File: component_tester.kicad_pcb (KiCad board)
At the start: 2 copper layers, 70 x 48 mm, 86 parts, among them IC1 ATMEGA16U2, IC2 ATMEGA328P-A, P1 USB_OTG, P10 ICSP_prog_16u2_4, P11 BO_PC6, P12 ICSP_prog_16u2_5, P13 BO_PC5, P14 BO_PD2, P15 BO_PD3, P16 BO_PD4, P17 BO_PD5, P18 BO_PD6, P19 ICSP_prog_328_1, P2 BATTERY_CONNECTOR, P20 ICSP_prog_328_3, P21 ICSP_prog_328_4, P22 ICSP_prog_328_5, P23 CONN_01X01, P24 Device Under Test, P25 CONN_01X03, P3 Voltage_for_zener, P4 BO_PC7, P5 ICSP_prog_16u2_1, P6 BO_PD0, P7 BO_PD1, P8 BO_PC4, P9 ICSP_prog_16u2_3, Q1 TRANSISTOR_NPN_2N2222_KSP222A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, SW1 ON-OFF switch, SW2 DO_MEASUREMENT, SW3 CONNECT_CAP, U1 NCP1117ST50T3G, U2 XF2L-2625-1A, U3 LT1004, U4 CDSOT23-SRV05-4, Y1 8MHz, Y2 16MHz

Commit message: Added screw holes
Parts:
- added REF**: 1pin, Connect:1pin, F.Cu at (165.1, 127.6)
- added REF**: 1pin, Connect:1pin, F.Cu at (131.7, 103.4)
- added REF**: 1pin, Connect:1pin, F.Cu at (112.9, 143.9)
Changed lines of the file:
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@@
 (kicad_pcb (version 4) (host pcbnew 4.0.2+e4-6225~38~ubuntu16.04.1-stable)
   (general
-    (links 193)
+    (links 196)
     (no_connects 3)
-    (area 99.949999 99.949999 170.050001 148.050001)
+    (area 93.753 93.596447 170.970334 149.9968)
     (thickness 1.6)
     (drawings 4)
     (tracks 1061)
     (zones 0)
-    (modules 86)
+    (modules 89)
     (nets 77)
   )
@@
     (mod_text_size 1 1)
     (mod_text_width 0.15)
-    (pad_size 1.5 1.5)
-    (pad_drill 0.6)
+    (pad_size 4.064 4.064)
+    (pad_drill 3.048)
     (pad_to_mask_clearance 0)
     (aux_axis_origin 0 0)
@@
     (add_net UART_328_TO_16u)
   )
+  (module Connect:1pin (layer F.Cu)
+    (at 165.1 127.635)
+    (descr "module 1 pin (ou trou mecanique de percage)")
+    (tags DEV)
+    (fp_text reference REF** (at 0 -3.048) (layer F.SilkS)
+      (effects (font (size 1 1) (thickness 0.15)))
+    )
+    (fp_text value 1pin (at 0 2.794) (layer F.Fab)
+      (effects (font (size 1 1) (thickness 0.15)))
+    )
+    (fp_circle (center 0 0) (end 0 -2.286) (layer F.SilkS) (width 0.15))
+    (pad 1 thru_hole circle (at 0 0) (size 4.064 4.064) (drill 3.048) (layers *.Cu *.Mask F.SilkS)
+      (net 1 GND))
+  )
+  (module Connect:1pin (layer F.Cu)
+    (at 131.699 103.378)
+    (descr "module 1 pin (ou trou mecanique de percage)")
+    (tags DEV)
+    (fp_text reference REF** (at 0 -3.048) (layer F.SilkS)
+      (effects (font (size 1 1) (thickness 0.15)))
+    )
+    (fp_text value 1pin (at 0 2.794) (layer F.Fab)
+      (effects (font (size 1 1) (thickness 0.15)))
+    )
+    (fp_circle (center 0 0) (end 0 -2.286) (layer F.SilkS) (width 0.15))
+    (pad 1 thru_hole circle (at 0 0) (size 4.064 4.064) (drill 3.048) (layers *.Cu *.Mask F.SilkS)
+      (net 1 GND))
+  )
   (module drawn_by_jpmeijers:CONN_DUT (layer F.Cu)
     (at 149.8092 135.2296)
@@
     )
   )
+  (module Connect:1pin (layer F.Cu)
+    (at 112.903 143.891)
+    (descr "module 1 pin (ou trou mecanique de percage)")
+    (tags DEV)
+    (fp_text reference REF** (at 0 -3.048) (layer F.SilkS)
+      (effects (font (size 1 1) (thickness 0.15)))
+    )
+    (fp_text value 1pin (at 0 2.794) (layer F.Fab)
+      (effects (font (size 1 1) (thickness 0.15)))
+    )
+    (fp_circle (center 0 0) (end 0 -2.286) (layer F.SilkS) (width 0.15))
+    (pad 1 thru_hole circle (at 0 0) (size 4.064 4.064) (drill 3.048) (layers *.Cu *.Mask F.SilkS)
+      (net 1 GND))
+  )
   (gr_line (start 100 148) (end 170 148) (angle 90) (layer Edge.Cuts) (width 0.1))
   (gr_line (start 170 100) (end 170 148) (angle 90) (layer Edge.Cuts) (width 0.1))
@@
   (segment (start 105.3592 110.998) (end 107.3912 108.966) (width 0.25) (layer F.Cu) (net 6))
   (segment (start 103.144 110.998) (end 105.3592 110.998) (width 0.25) (layer F.Cu) (net 6))
-  (segment (start 140.335 130.957) (end 140.335 129.5146) (width 0.25) (layer B.Cu) (net 7) (status 400000))
+  (segment (start 140.335 130.957) (end 140.335 129.5146) (width 0.25) (layer B.Cu) (net 7))
   (segment (start 140.335 129.5146) (end 140.6144 129.2352) (width 0.25) (layer B.Cu) (net 7))
   (segment (start 138.75 132.715) (end 138.75 131.0996) (width 0.25) (layer F.Cu) (net 7))

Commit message: Fix capacitor values Added Vusb cap, fix unconnected nets, better grounding.
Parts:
- added C21: 100n, Capacitors_SMD:C_0805_HandSoldering, B.Cu at (131.1, 115.4)
- C10, C9: value 10uF -> 10u
- C15, C16: value 22pF -> 22p
- C3: value 1uF -> 1u
- moved U4 0.11 mm to (153.5, 132.5)
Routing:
- net /Reference_voltage: track 32.8 -> 35.9 mm
- net /RESET_16u: track 6.27 -> 9.16 mm
- net GND: track 576.6 -> 579.5 mm, vias 125 -> 126
- net /USB_Vcc: track 52.0 -> 53.8 mm, vias 4 -> 5
- net UART_328_TO_16u: track 58.2 -> 58.8 mm
- net /LCD_DATA_B2: track 12.5 -> 11.9 mm

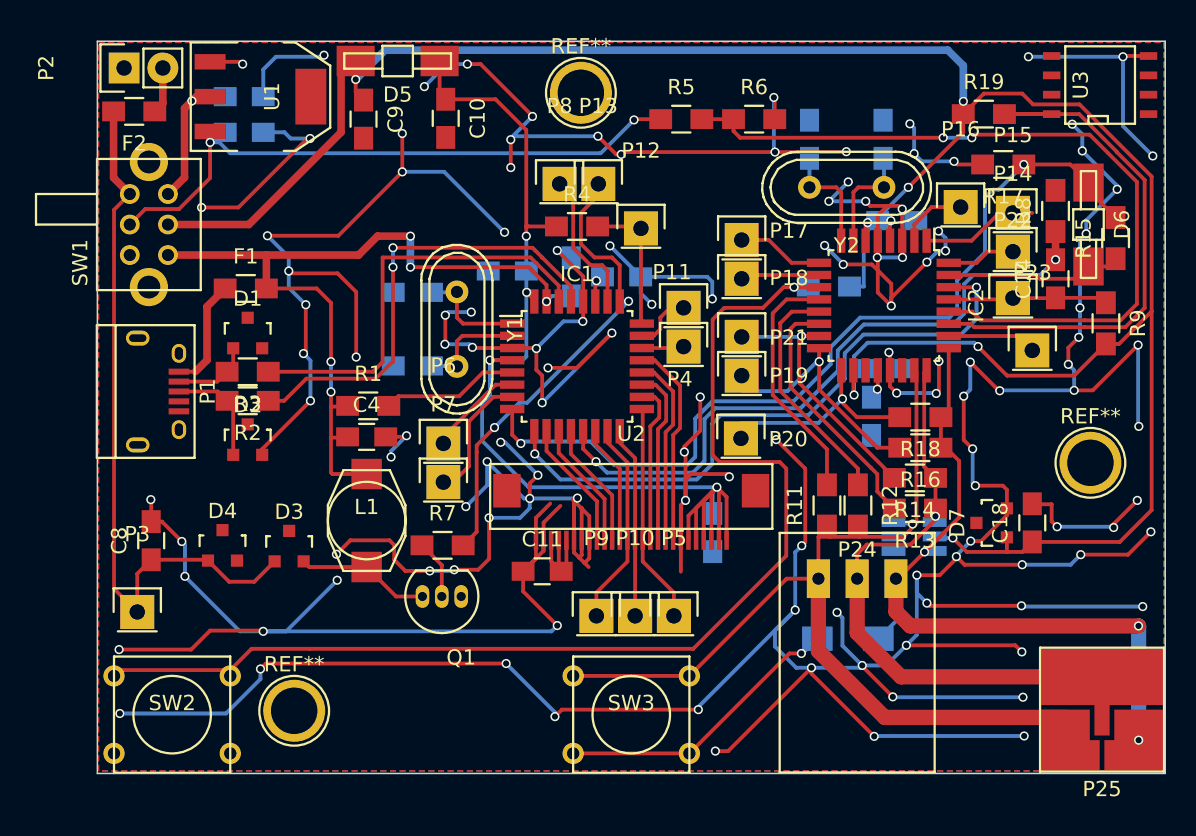
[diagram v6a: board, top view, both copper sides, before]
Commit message: Move component references on silkscreen to be more readable.
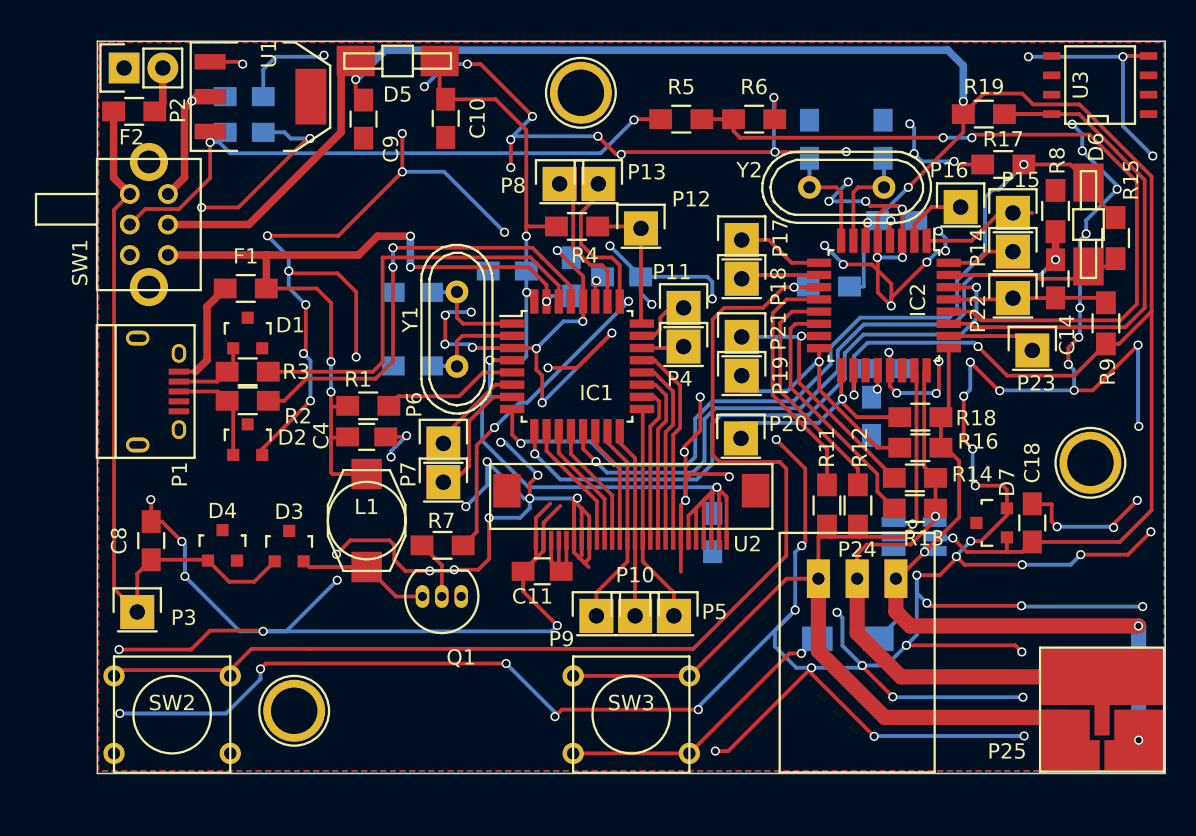
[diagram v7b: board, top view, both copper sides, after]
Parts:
- renumbered REF** to ?

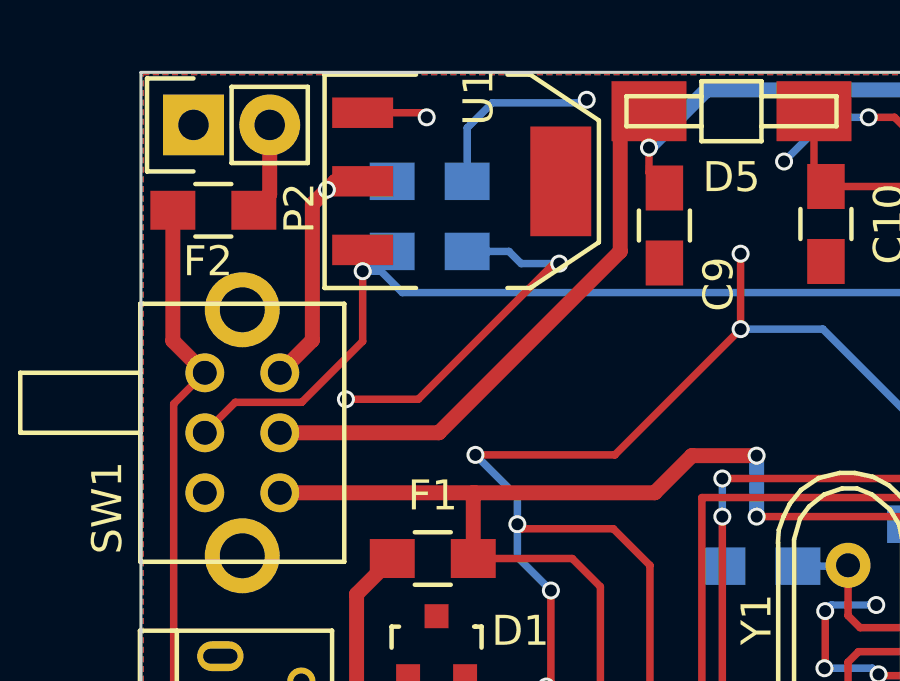
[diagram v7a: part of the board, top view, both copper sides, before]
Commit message: Added voltage regulator option
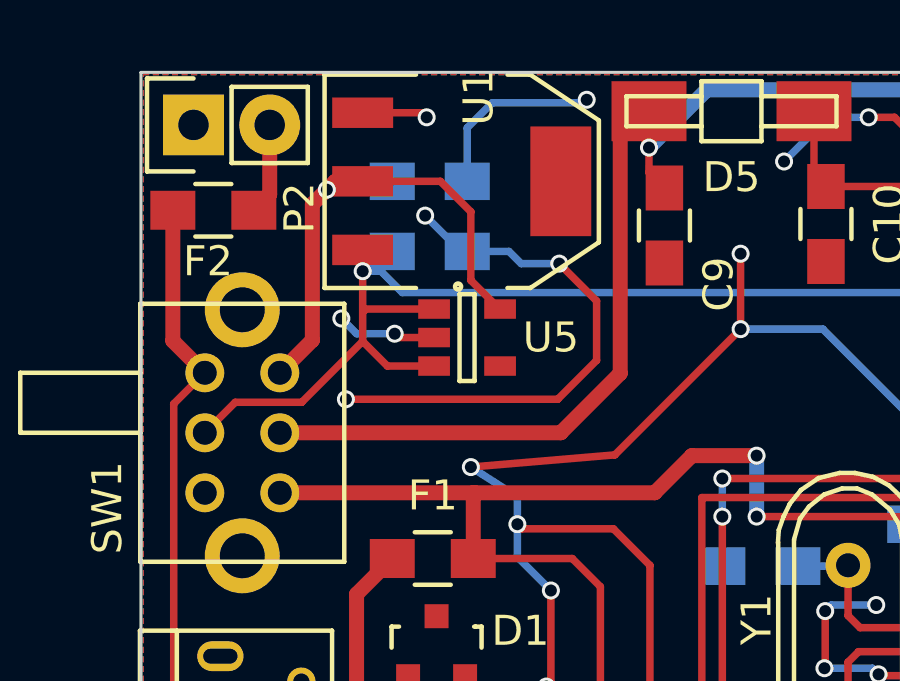
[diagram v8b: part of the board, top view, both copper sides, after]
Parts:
- added U5: LP2985LV, TO_SOT_Packages_SMD:SOT-23-5, F.Cu at (110.9, 108.8)
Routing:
- net GND: track 579.5 -> 588.6 mm, vias 126 -> 129
- net /Volt_reg_5v: track 10.4 -> 18.0 mm
- net Batt_Switch: track 41.6 -> 46.8 mm
- net 5Volt_328: track 168.3 -> 170.7 mm
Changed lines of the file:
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@@
 (kicad_pcb (version 4) (host pcbnew 4.0.2+e4-6225~38~ubuntu16.04.1-stable)
   (general
-    (links 198)
+    (links 202)
     (no_connects 1)
-    (area 93.753 93.596447 170.970334 149.9968)
+    (area 99.949999 99.949999 170.050001 148.050001)
     (thickness 1.6)
     (drawings 4)
-    (tracks 1071)
+    (tracks 1094)
     (zones 0)
-    (modules 90)
-    (nets 77)
+    (modules 91)
+    (nets 78)
   )
   (page A4)
@@
   (net 75 "Net-(U4-Pad1)")
   (net 76 Battery_fused)
+  (net 77 "Net-(U5-Pad4)")
   (net_class Default "This is the default net class."
     (clearance 0.2)
@@
     (add_net "Net-(U3-Pad7)")
     (add_net "Net-(U4-Pad1)")
+    (add_net "Net-(U5-Pad4)")
     (add_net UART_16u_TO_328)
     (add_net UART_328_TO_16u)
@@
     )
   )
+  (module TO_SOT_Packages_SMD:SOT-23-5 (layer F.Cu)
+    (at 110.871 108.839)
+    (descr "5-pin SOT23 package")
+    (tags SOT-23-5)
+    (attr smd)
+    (fp_text reference U5 (at 2.794 0) (layer F.SilkS)
+      (effects (font (size 1 1) (thickness 0.15)))
+    )
+    (fp_text value LP2985LV (at -0.05 2.35) (layer F.Fab)
+      (effects (font (size 1 1) (thickness 0.15)))
+    )
+    (fp_line (start -1.8 -1.6) (end 1.8 -1.6) (layer F.CrtYd) (width 0.05))
+    (fp_line (start 1.8 -1.6) (end 1.8 1.6) (layer F.CrtYd) (width 0.05))
+    (fp_line (start 1.8 1.6) (end -1.8 1.6) (layer F.CrtYd) (width 0.05))
+    (fp_line (start -1.8 1.6) (end -1.8 -1.6) (layer F.CrtYd) (width 0.05))
+    (fp_circle (center -0.3 -1.7) (end -0.2 -1.7) (layer F.SilkS) (width 0.15))
+    (fp_line (start 0.25 -1.45) (end -0.25 -1.45) (layer F.SilkS) (width 0.15))
+    (fp_line (start 0.25 1.45) (end 0.25 -1.45) (layer F.SilkS) (width 0.15))
+    (fp_line (start -0.25 1.45) (end 0.25 1.45) (layer F.SilkS) (width 0.15))
+    (fp_line (start -0.25 -1.45) (end -0.25 1.45) (layer F.SilkS) (width 0.15))
+    (pad 1 smd rect (at -1.1 -0.95) (size 1.06 0.65) (layers F.Cu F.Paste F.Mask)
+      (net 6 Batt_Switch))
+    (pad 2 smd rect (at -1.1 0) (size 1.06 0.65) (layers F.Cu F.Paste F.Mask)
+      (net 1 GND))
+    (pad 3 smd rect (at -1.1 0.95) (size 1.06 0.65) (layers F.Cu F.Paste F.Mask)
+      (net 6 Batt_Switch))
+    (pad 4 smd rect (at 1.1 0.95) (size 1.06 0.65) (layers F.Cu F.Paste F.Mask)
+      (net 77 "Net-(U5-Pad4)"))
+    (pad 5 smd rect (at 1.1 -0.95) (size 1.06 0.65) (layers F.Cu F.Paste F.Mask)
+      (net 8 /Volt_reg_5v))
+    (model TO_SOT_Packages_SMD.3dshapes/SOT-23-5.wrl
+      (at (xyz 0 0 0))
+      (scale (xyz 1 1 1))
+      (rotate (xyz 0 0 0))
+    )
+  )
   (gr_line (start 100 148) (end 170 148) (angle 90) (layer Edge.Cuts) (width 0.1))
   (gr_line (start 170 100) (end 170 148) (angle 90) (layer Edge.Cuts) (width 0.1))
   (gr_line (start 100 100) (end 100 148) (angle 90) (layer Edge.Cuts) (width 0.1))
   (gr_line (start 100 100) (end 170 100) (angle 90) (layer Edge.Cuts) (width 0.1))
+  (segment (start 110.8764 105.9688) (end 110.6678 105.9688) (width 0.25) (layer B.Cu) (net 1))
+  (segment (start 110.6678 105.9688) (end 109.474 104.775) (width 0.25) (layer B.Cu) (net 1))
+  (via (at 109.474 104.775) (size 0.6) (drill 0.4) (layers F.Cu B.Cu) (net 1))
+  (segment (start 108.458 108.712) (end 107.188 108.712) (width 0.25) (layer B.Cu) (net 1))
+  (segment (start 108.585 108.839) (end 108.458 108.712) (width 0.25) (layer F.Cu) (net 1))
+  (via (at 108.458 108.712) (size 0.6) (drill 0.4) (layers F.Cu B.Cu) (net 1))
+  (segment (start 109.771 108.839) (end 108.585 108.839) (width 0.25) (layer F.Cu) (net 1))
+  (via (at 106.68 108.204) (size 0.6) (drill 0.4) (layers F.Cu B.Cu) (net 1))
+  (segment (start 107.188 108.712) (end 106.68 108.204) (width 0.25) (layer B.Cu) (net 1))
+  (segment (start 106.8324 110.8964) (end 113.8936 110.8964) (width 0.25) (layer F.Cu) (net 1))
+  (via (at 106.8324 110.8964) (size 0.6) (drill 0.4) (layers F.Cu B.Cu) (net 1))
+  (segment (start 115.189 107.6198) (end 113.9444 106.3752) (width 0.25) (layer F.Cu) (net 1))
+  (segment (start 115.189 109.601) (end 115.189 107.6198) (width 0.25) (layer F.Cu) (net 1))
+  (segment (start 113.8936 110.8964) (end 115.189 109.601) (width 0.25) (layer F.Cu) (net 1))
   (segment (start 135.616 115.443) (end 135.616 115.423) (width 0.25) (layer B.Cu) (net 1))
   (segment (start 135.616 115.423) (end 133.604 113.411) (width 0.25) (layer B.Cu) (net 1))
@@
   (via (at 113.9444 106.3752) (size 0.6) (drill 0.4) (layers F.Cu B.Cu) (net 1))
   (segment (start 110.8764 105.9688) (end 112.268 105.9688) (width 0.25) (layer B.Cu) (net 1))
-  (via (at 106.8324 110.8964) (size 0.6) (drill 0.4) (layers F.Cu B.Cu) (net 1))
-  (segment (start 109.2454 110.8964) (end 106.8324 110.8964) (width 0.25) (layer F.Cu) (net 1))
-  (segment (start 113.7666 106.3752) (end 109.2454 110.8964) (width 0.25) (layer F.Cu) (net 1))
   (segment (start 107.3912 101.346) (end 109.3724 101.346) (width 0.25) (layer F.Cu) (net 1))
   (via (at 109.5248 101.4984) (size 0.6) (drill 0.4) (layers F.Cu B.Cu) (net 1))
@@
   (segment (start 115.7986 112.7506) (end 119.9896 108.5596) (width 0.25) (layer F.Cu) (net 1))
   (segment (start 112.5474 114.1476) (end 112.5474 115.062) (width 0.25) (layer B.Cu) (net 1))
-  (via (at 111.1504 112.7506) (size 0.6) (drill 0.4) (layers F.Cu B.Cu) (net 1))
-  (segment (start 112.5474 114.1476) (end 111.1504 112.7506) (width 0.25) (layer B.Cu) (net 1))
-  (segment (start 111.1504 112.7506) (end 115.7986 112.7506) (width 0.25) (layer F.Cu) (net 1))
+  (via (at 110.998 113.157) (size 0.6) (drill 0.4) (layers F.Cu B.Cu) (net 1))
+  (segment (start 112.5474 114.1476) (end 110.998 113.157) (width 0.25) (layer B.Cu) (net 1))
+  (segment (start 110.998 113.157) (end 115.7986 112.7506) (width 0.25) (layer F.Cu) (net 1))
   (via (at 119.9896 106.045) (size 0.6) (drill 0.4) (layers F.Cu B.Cu) (net 1))
   (segment (start 113.9698 123.571) (end 113.9698 120.9294) (width 0.25) (layer B.Cu) (net 1))
@@
   (segment (start 129.445 115.983) (end 128.5875 115.1255) (width 0.25) (layer F.Cu) (net 5))
   (segment (start 128.5875 115.1255) (end 128.524 115.062) (width 0.25) (layer F.Cu) (net 5))
+  (segment (start 109.771 109.789) (end 108.2142 109.789) (width 0.25) (layer F.Cu) (net 6))
+  (segment (start 108.2142 109.789) (end 107.3912 108.966) (width 0.25) (layer F.Cu) (net 6))
+  (segment (start 109.771 107.889) (end 107.3912 107.889) (width 0.25) (layer F.Cu) (net 6))
+  (segment (start 107.442 107.95) (end 107.3912 107.95) (width 0.25) (layer F.Cu) (net 6))
+  (segment (start 107.442 107.9398) (end 107.442 107.95) (width 0.25) (layer F.Cu) (net 6))
+  (segment (start 107.3912 107.889) (end 107.442 107.9398) (width 0.25) (layer F.Cu) (net 6))
   (segment (start 107.3912 106.6292) (end 108.0008 106.6292) (width 0.25) (layer B.Cu) (net 6))
   (segment (start 135.2296 105.1052) (end 136.9276 105.1052) (width 0.25) (layer F.Cu) (net 6))
@@
   (segment (start 108.0516 105.9688) (end 108.3764 105.9688) (width 0.25) (layer B.Cu) (net 6))
   (segment (start 102.128 112.014) (end 103.144 110.998) (width 0.25) (layer F.Cu) (net 6))
-  (segment (start 107.3912 108.966) (end 107.3912 106.6292) (width 0.25) (layer F.Cu) (net 6))
+  (segment (start 107.3912 108.966) (end 107.3912 107.95) (width 0.25) (layer F.Cu) (net 6))
+  (segment (start 107.3912 107.95) (end 107.3912 106.6292) (width 0.25) (layer F.Cu) (net 6))
   (segment (start 107.3912 106.6292) (end 107.3912 105.918) (width 0.25) (layer F.Cu) (net 6))
   (segment (start 105.3592 110.998) (end 107.3912 108.966) (width 0.25) (layer F.Cu) (net 6))
@@
   (segment (start 128.651 115.316) (end 128.397 115.062) (width 0.25) (layer B.Cu) (net 7))
   (segment (start 128.397 115.062) (end 128.123 115.062) (width 0.25) (layer B.Cu) (net 7))
+  (segment (start 111.971 107.889) (end 111.953 107.889) (width 0.25) (layer F.Cu) (net 8))
+  (segment (start 111.953 107.889) (end 110.998 106.934) (width 0.25) (layer F.Cu) (net 8))
+  (segment (start 110.998 106.934) (end 110.998 104.648) (width 0.25) (layer F.Cu) (net 8))
+  (segment (start 110.998 104.648) (end 109.982 103.632) (width 0.25) (layer F.Cu) (net 8))
+  (segment (start 109.982 103.632) (end 107.3912 103.632) (width 0.25) (layer F.Cu) (net 8))
   (via (at 106.1974 103.9114) (size 0.6) (drill 0.4) (layers F.Cu B.Cu) (net 8))
   (segment (start 108.3764 103.632) (end 106.4768 103.632) (width 0.25) (layer B.Cu) (net 8))
@@
   (segment (start 116.9348 101.2952) (end 116.9348 103.3404) (width 0.25) (layer F.Cu) (net 10))
   (segment (start 116.9348 103.3404) (end 117.4496 103.8552) (width 0.25) (layer F.Cu) (net 10))
-  (segment (start 104.628 112.014) (end 109.9312 112.014) (width 0.5) (layer F.Cu) (net 10))
-  (segment (start 109.9312 112.014) (end 115.9764 105.9688) (width 0.5) (layer F.Cu) (net 10))
-  (segment (start 115.9764 105.9688) (end 115.9764 102.2536) (width 0.5) (layer F.Cu) (net 10))
+  (segment (start 104.628 112.014) (end 113.9952 112.014) (width 0.5) (layer F.Cu) (net 10))
+  (segment (start 113.9952 112.014) (end 115.9764 110.0328) (width 0.5) (layer F.Cu) (net 10))
+  (segment (start 115.9764 110.0328) (end 115.9764 102.2536) (width 0.5) (layer F.Cu) (net 10))
   (segment (start 115.9764 102.2536) (end 116.9348 101.2952) (width 0.25) (layer F.Cu) (net 10))
   (segment (start 169.1132 108.8644) (end 164.3888 104.14) (width 0.25) (layer F.Cu) (net 10))
